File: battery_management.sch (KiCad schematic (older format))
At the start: 8 parts

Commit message: Finally finished final draft
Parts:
- gave numbers to parts that had none: 8
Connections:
- net charging/VCC_IN_USB renamed charging_ic/VCC_IN_USB
- net fuel_gage/VCC_BAT renamed fuel_gage_ic/VCC_BAT
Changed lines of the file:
@@
 P 7100 2900
 AR Path="/60C0E79E" Ref="C?"  Part="1"
-AR Path="/60BA4931/60C0E79E" Ref="C?"  Part="1"
-F 0 "C?" H 7215 2946 50  0000 L CNN
+AR Path="/60BA4931/60C0E79E" Ref="C7"  Part="1"
+F 0 "C7" H 7215 2946 50  0000 L CNN
 F 1 "0.1uF" H 7215 2855 50  0000 L CNN
 F 2 "" H 7138 2750 50  0001 C CNN
@@
 P 7650 2900
 AR Path="/60C0E7AB" Ref="C?"  Part="1"
-AR Path="/60BA4931/60C0E7AB" Ref="C?"  Part="1"
-F 0 "C?" H 7765 2946 50  0000 L CNN
+AR Path="/60BA4931/60C0E7AB" Ref="C6"  Part="1"
+F 0 "C6" H 7765 2946 50  0000 L CNN
 F 1 "10uF" H 7765 2855 50  0000 L CNN
 F 2 "" H 7688 2750 50  0001 C CNN
@@
 P 8150 2900
 AR Path="/60C0E7BA" Ref="C?"  Part="1"
-AR Path="/60BA4931/60C0E7BA" Ref="C?"  Part="1"
-F 0 "C?" H 8265 2946 50  0000 L CNN
+AR Path="/60BA4931/60C0E7BA" Ref="C5"  Part="1"
+F 0 "C5" H 8265 2946 50  0000 L CNN
 F 1 "10uF" H 8265 2855 50  0000 L CNN
 F 2 "" H 8188 2750 50  0001 C CNN
@@
 P 8700 2900
 AR Path="/60C0E7C0" Ref="C?"  Part="1"
-AR Path="/60BA4931/60C0E7C0" Ref="C?"  Part="1"
-F 0 "C?" H 8815 2946 50  0000 L CNN
+AR Path="/60BA4931/60C0E7C0" Ref="C4"  Part="1"
+F 0 "C4" H 8815 2946 50  0000 L CNN
 F 1 "0.1uF" H 8815 2855 50  0000 L CNN
 F 2 "" H 8738 2750 50  0001 C CNN
@@
 P 7900 2600
 AR Path="/60C0E7D7" Ref="FB?"  Part="1"
-AR Path="/60BA4931/60C0E7D7" Ref="FB?"  Part="1"
-F 0 "FB?" V 7626 2600 50  0000 C CNN
+AR Path="/60BA4931/60C0E7D7" Ref="FB1"  Part="1"
+F 0 "FB1" V 7626 2600 50  0000 C CNN
 F 1 "FerriteBead" V 7717 2600 50  0000 C CNN
 F 2 "" V 7830 2600 50  0001 C CNN
@@
 F3 "VCC_IN" I L 5700 3400 50
 $EndSheet
-$Sheet
-S 2400 3100 1150 1350
-U 60C6FA96
-F0 "fuel_gage" 50
-F1 "fuel_gage.sch" 50
-F2 "VCC_3V3" I R 3550 3850 50
-F3 "GPOUT" O R 3550 4050 50
-F4 "SCL" I R 3550 4250 50
-F5 "SDA" B R 3550 4150 50
-F6 "VCC_BAT" B L 2400 3750 50
-F7 "VCC_LOAD_OR_CHARGE" B R 3550 3300 50
-$EndSheet
-$Sheet
-S 4050 2450 1100 550
-U 60C34886
-F0 "charging" 50
-F1 "charging.sch" 50
-F2 "VCC_LOAD" O R 5150 2600 50
-F3 "VCC_IN_USB" I L 4050 2600 50
-F4 "VCC_BAT_OR_CHARGE" B L 4050 2850 50
-$EndSheet
 Wire Wire Line
 	5150 2600 5400 2600
@@
 P 1750 3850
 AR Path="/60C8C86F" Ref="J?"  Part="1"
-AR Path="/60BA4931/60C8C86F" Ref="J?"  Part="1"
+AR Path="/60BA4931/60C8C86F" Ref="J7"  Part="1"
 AR Path="/60BA4931/60C6FA96/60C8C86F" Ref="J?"  Part="1"
-F 0 "J?" H 1668 3525 50  0000 C CNN
+F 0 "J7" H 1668 3525 50  0000 C CNN
 F 1 "Battery_175mAh" H 1668 3616 50  0000 C CNN
 F 2 "" H 1750 3850 50  0001 C CNN
@@
 P 1800 1650
 AR Path="/60C9133A" Ref="J?"  Part="1"
-AR Path="/60BA4931/60C9133A" Ref="J?"  Part="1"
+AR Path="/60BA4931/60C9133A" Ref="J6"  Part="1"
 AR Path="/60BA4931/60C34886/60C9133A" Ref="J?"  Part="1"
-F 0 "J?" H 1857 2117 50  0000 C CNN
+F 0 "J6" H 1857 2117 50  0000 C CNN
 F 1 "USB_B_Micro" H 1857 2026 50  0000 C CNN
 F 2 "" H 1950 1600 50  0001 C CNN
@@
 P 2450 1750
 AR Path="/60C91355" Ref="D?"  Part="1"
-AR Path="/60BA4931/60C91355" Ref="D?"  Part="1"
+AR Path="/60BA4931/60C91355" Ref="D1"  Part="1"
 AR Path="/60BA4931/60C34886/60C91355" Ref="D?"  Part="1"
-F 0 "D?" V 2404 1880 50  0000 L CNN
+F 0 "D1" V 2404 1880 50  0000 L CNN
 F 1 "SMAJ5.0A" V 2495 1880 50  0000 L CNN
 F 2 "DIOM5026X229N" H 2200 1500 50  0001 L CNN
@@
 Text HLabel 9000 2600 2    50   Output ~ 0
 VCC_POWER
+Wire Wire Line
+	3550 4050 3950 4050
+Wire Wire Line
+	3550 4150 3950 4150
+Wire Wire Line
+	3550 4250 3950 4250
+Text HLabel 3950 4050 2    50   Output ~ 0
+GPOUT
+Text HLabel 3950 4150 2    50   BiDi ~ 0
+SDA
+Text HLabel 3950 4250 2    50   Input ~ 0
+SCL
+$Sheet
+S 4050 2450 1100 550
+U 60C34886
+F0 "charging_ic" 50
+F1 "charging_ic.sch" 50
+F2 "VCC_LOAD" O R 5150 2600 50
+F3 "VCC_IN_USB" I L 4050 2600 50
+F4 "VCC_BAT_OR_CHARGE" B L 4050 2850 50
+$EndSheet
+$Sheet
+S 2400 3100 1150 1350
+U 60C6FA96
+F0 "fuel_gage_ic" 50
+F1 "fuel_gage_ic.sch" 50
+F2 "VCC_3V3" I R 3550 3850 50
+F3 "GPOUT" O R 3550 4050 50
+F4 "SCL" I R 3550 4250 50
+F5 "SDA" B R 3550 4150 50
+F6 "VCC_BAT" B L 2400 3750 50
+F7 "VCC_LOAD_OR_CHARGE" B R 3550 3300 50
+$EndSheet
 $EndSCHEMATC

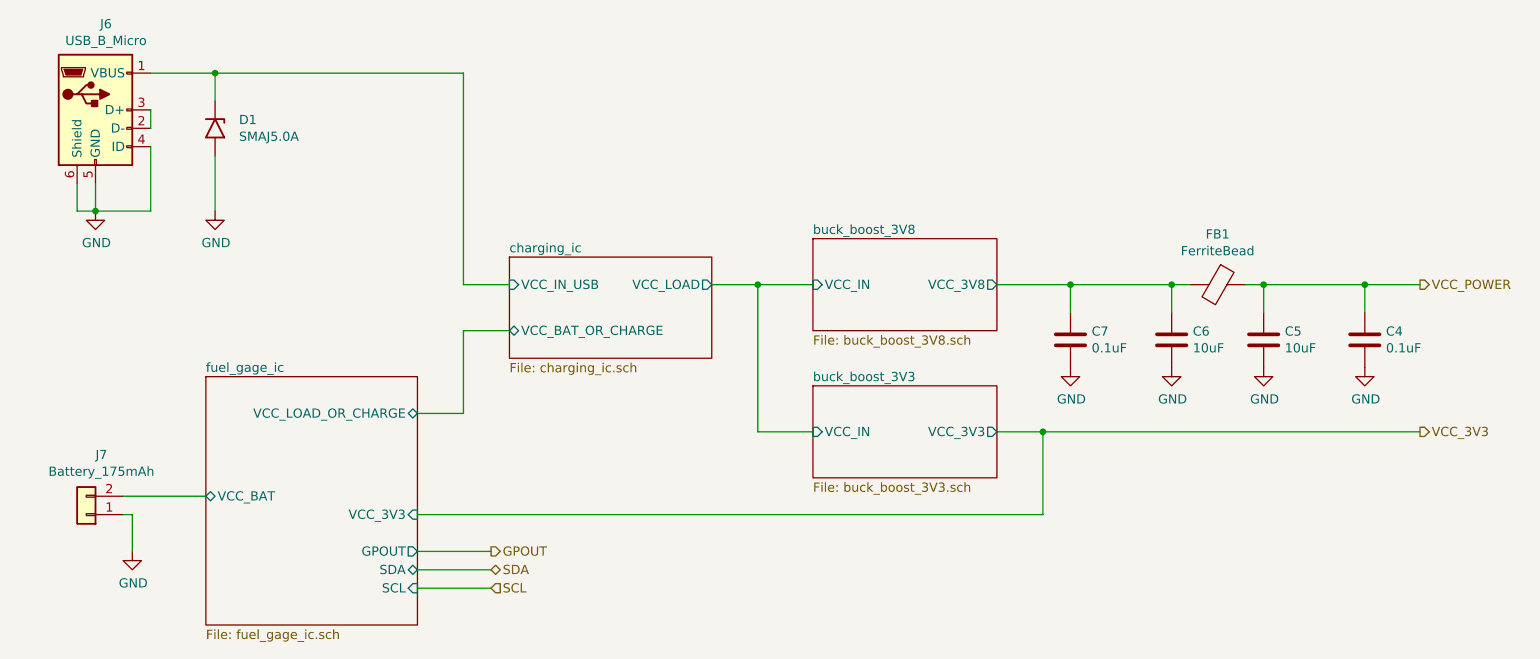
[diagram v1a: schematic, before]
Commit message: Fixed some symbols, assigned some footprints, and made wire labels
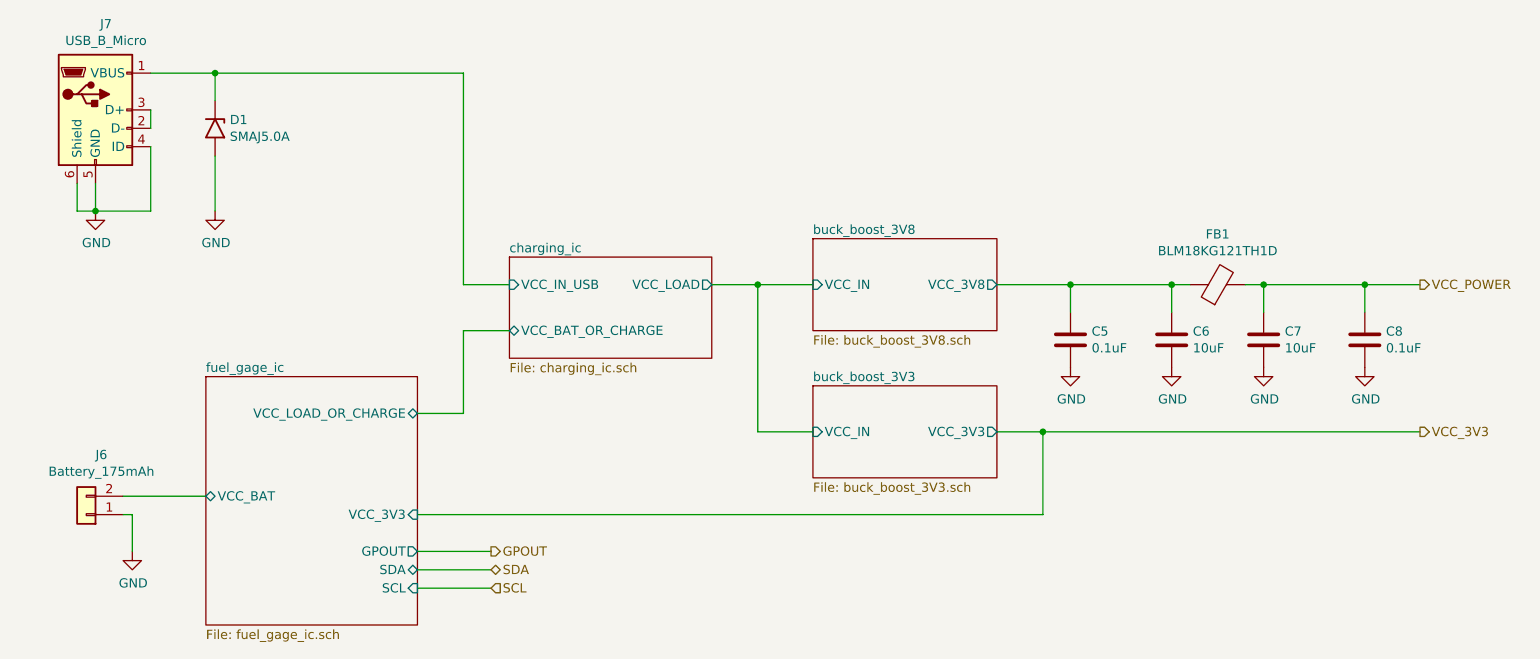
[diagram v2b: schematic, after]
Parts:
- removed FB1: FerriteBead, symbol Device:FerriteBead
- added FB1: BLM18KG121TH1D, Ferrite_Skywire:BLM18KG101TH1D, symbol Ferrite_Bead:BLM18KG121TH1D
- D1: footprint DIOM5026X229N -> Diode_Skywire:DIOM5026X229N
- renumbered C7 to C5, C5 to C7, C4 to C8, J7 to J6, J6 to J7
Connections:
- net VCC_POWER: now also FB1.2
- net buck_boost_3V8/VCC_3V8: now also FB1.1
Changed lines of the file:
@@
 P 7100 2900
 AR Path="/60C0E79E" Ref="C?"  Part="1"
-AR Path="/60BA4931/60C0E79E" Ref="C7"  Part="1"
-F 0 "C7" H 7215 2946 50  0000 L CNN
+AR Path="/60BA4931/60C0E79E" Ref="C5"  Part="1"
+F 0 "C5" H 7215 2946 50  0000 L CNN
 F 1 "0.1uF" H 7215 2855 50  0000 L CNN
 F 2 "" H 7138 2750 50  0001 C CNN
@@
 P 7100 3050
 AR Path="/60C0E7A4" Ref="#PWR?"  Part="1"
-AR Path="/60BA4931/60C0E7A4" Ref="#PWR?"  Part="1"
-F 0 "#PWR?" H 7100 2800 50  0001 C CNN
+AR Path="/60BA4931/60C0E7A4" Ref="#PWR012"  Part="1"
+F 0 "#PWR012" H 7100 2800 50  0001 C CNN
 F 1 "GND" H 7105 2877 50  0000 C CNN
 F 2 "" H 7100 3050 50  0001 C CNN
@@
 P 7650 3050
 AR Path="/60C0E7B1" Ref="#PWR?"  Part="1"
-AR Path="/60BA4931/60C0E7B1" Ref="#PWR?"  Part="1"
-F 0 "#PWR?" H 7650 2800 50  0001 C CNN
+AR Path="/60BA4931/60C0E7B1" Ref="#PWR013"  Part="1"
+F 0 "#PWR013" H 7650 2800 50  0001 C CNN
 F 1 "GND" H 7655 2877 50  0000 C CNN
 F 2 "" H 7650 3050 50  0001 C CNN
@@
 P 8150 2900
 AR Path="/60C0E7BA" Ref="C?"  Part="1"
-AR Path="/60BA4931/60C0E7BA" Ref="C5"  Part="1"
-F 0 "C5" H 8265 2946 50  0000 L CNN
+AR Path="/60BA4931/60C0E7BA" Ref="C7"  Part="1"
+F 0 "C7" H 8265 2946 50  0000 L CNN
 F 1 "10uF" H 8265 2855 50  0000 L CNN
 F 2 "" H 8188 2750 50  0001 C CNN
@@
 P 8700 2900
 AR Path="/60C0E7C0" Ref="C?"  Part="1"
-AR Path="/60BA4931/60C0E7C0" Ref="C4"  Part="1"
-F 0 "C4" H 8815 2946 50  0000 L CNN
+AR Path="/60BA4931/60C0E7C0" Ref="C8"  Part="1"
+F 0 "C8" H 8815 2946 50  0000 L CNN
 F 1 "0.1uF" H 8815 2855 50  0000 L CNN
 F 2 "" H 8738 2750 50  0001 C CNN
@@
 P 8150 3050
 AR Path="/60C0E7C6" Ref="#PWR?"  Part="1"
-AR Path="/60BA4931/60C0E7C6" Ref="#PWR?"  Part="1"
-F 0 "#PWR?" H 8150 2800 50  0001 C CNN
+AR Path="/60BA4931/60C0E7C6" Ref="#PWR014"  Part="1"
+F 0 "#PWR014" H 8150 2800 50  0001 C CNN
 F 1 "GND" H 8155 2877 50  0000 C CNN
 F 2 "" H 8150 3050 50  0001 C CNN
@@
 P 8700 3050
 AR Path="/60C0E7CC" Ref="#PWR?"  Part="1"
-AR Path="/60BA4931/60C0E7CC" Ref="#PWR?"  Part="1"
-F 0 "#PWR?" H 8700 2800 50  0001 C CNN
+AR Path="/60BA4931/60C0E7CC" Ref="#PWR015"  Part="1"
+F 0 "#PWR015" H 8700 2800 50  0001 C CNN
 F 1 "GND" H 8705 2877 50  0000 C CNN
 F 2 "" H 8700 3050 50  0001 C CNN
@@
 Wire Wire Line
 	8700 2600 9000 2600
-$Comp
-L Device:FerriteBead FB?
-U 1 1 60C0E7D7
-P 7900 2600
-AR Path="/60C0E7D7" Ref="FB?"  Part="1"
-AR Path="/60BA4931/60C0E7D7" Ref="FB1"  Part="1"
-F 0 "FB1" V 7626 2600 50  0000 C CNN
-F 1 "FerriteBead" V 7717 2600 50  0000 C CNN
-F 2 "" V 7830 2600 50  0001 C CNN
-F 3 "~" H 7900 2600 50  0001 C CNN
-	1    7900 2600
-	0    1    1    0
-$EndComp
 Wire Wire Line
 	8050 2600 8150 2600
@@
 P 1750 3850
 AR Path="/60C8C86F" Ref="J?"  Part="1"
-AR Path="/60BA4931/60C8C86F" Ref="J7"  Part="1"
+AR Path="/60BA4931/60C8C86F" Ref="J6"  Part="1"
 AR Path="/60BA4931/60C6FA96/60C8C86F" Ref="J?"  Part="1"
-F 0 "J7" H 1668 3525 50  0000 C CNN
+F 0 "J6" H 1668 3525 50  0000 C CNN
 F 1 "Battery_175mAh" H 1668 3616 50  0000 C CNN
 F 2 "" H 1750 3850 50  0001 C CNN
@@
 	2000 3850 2000 4050
 $Comp
-L power:GND #PWR?
+L power:GND #PWR010
 U 1 1 60C8D052
 P 2000 4050
-F 0 "#PWR?" H 2000 3800 50  0001 C CNN
+F 0 "#PWR010" H 2000 3800 50  0001 C CNN
 F 1 "GND" H 2005 3877 50  0000 C CNN
 F 2 "" H 2000 4050 50  0001 C CNN
@@
 P 1800 1650
 AR Path="/60C9133A" Ref="J?"  Part="1"
-AR Path="/60BA4931/60C9133A" Ref="J6"  Part="1"
+AR Path="/60BA4931/60C9133A" Ref="J7"  Part="1"
 AR Path="/60BA4931/60C34886/60C9133A" Ref="J?"  Part="1"
-F 0 "J6" H 1857 2117 50  0000 C CNN
+F 0 "J7" H 1857 2117 50  0000 C CNN
 F 1 "USB_B_Micro" H 1857 2026 50  0000 C CNN
 F 2 "" H 1950 1600 50  0001 C CNN
@@
 P 1800 2200
 AR Path="/60C91347" Ref="#PWR?"  Part="1"
-AR Path="/60BA4931/60C91347" Ref="#PWR?"  Part="1"
+AR Path="/60BA4931/60C91347" Ref="#PWR09"  Part="1"
 AR Path="/60BA4931/60C34886/60C91347" Ref="#PWR?"  Part="1"
-F 0 "#PWR?" H 1800 1950 50  0001 C CNN
+F 0 "#PWR09" H 1800 1950 50  0001 C CNN
 F 1 "GND" H 1805 2027 50  0000 C CNN
 F 2 "" H 1800 2200 50  0001 C CNN
@@
 	1    0    0    -1
 $EndComp
-$Comp
-L Diode_TVS:SMAJ5.0A D?
-U 1 1 60C91355
-P 2450 1750
-AR Path="/60C91355" Ref="D?"  Part="1"
-AR Path="/60BA4931/60C91355" Ref="D1"  Part="1"
-AR Path="/60BA4931/60C34886/60C91355" Ref="D?"  Part="1"
-F 0 "D1" V 2404 1880 50  0000 L CNN
-F 1 "SMAJ5.0A" V 2495 1880 50  0000 L CNN
-F 2 "DIOM5026X229N" H 2200 1500 50  0001 L CNN
-F 3 "https://detail.tmall.com/item.htm?id=548354020241&ali_refid=a3_430583_1006:1109983619:N:3Uw9kZ3UMDT/QL57nh1fXA==:ab063b49c94624768a940a913313feb0&ali_trackid=1_ab063b49c94624768a940a913313feb0&spm=a230r.1.14.1" H 2200 1400 50  0001 L CNN
-F 4 "BOURNS - SMAJ5.0A - TVS Diode, TRANSZORB SMAJ Series, Unidirectional, 5 V, 9.2 V, DO-214AC (SMA), 2 Pins" H 2200 1300 50  0001 L CNN "Description"
-F 5 "2.29" H 2200 1200 50  0001 L CNN "Height"
-F 6 "Bourns" H 2200 1100 50  0001 L CNN "Manufacturer_Name"
-F 7 "SMAJ5.0A" H 2200 1000 50  0001 L CNN "Manufacturer_Part_Number"
-F 8 "652-SMAJ5.0A" H 2200 900 50  0001 L CNN "Mouser Part Number"
-F 9 "https://www.mouser.co.uk/ProductDetail/Bourns/SMAJ50A?qs=A3H9pljuJ8RbLIvzFxDfUA%3D%3D" H 2200 800 50  0001 L CNN "Mouser Price/Stock"
-F 10 "SMAJ5.0A" H 2200 700 50  0001 L CNN "Arrow Part Number"
-F 11 "https://www.arrow.com/en/products/smaj5.0a/bourns" H 2200 600 50  0001 L CNN "Arrow Price/Stock"
-	1    2450 1750
-	0    1    1    0
-$EndComp
 Wire Wire Line
 	2450 1450 2450 1600
@@
 P 2450 2200
 AR Path="/60C9135D" Ref="#PWR?"  Part="1"
-AR Path="/60BA4931/60C9135D" Ref="#PWR?"  Part="1"
+AR Path="/60BA4931/60C9135D" Ref="#PWR011"  Part="1"
 AR Path="/60BA4931/60C34886/60C9135D" Ref="#PWR?"  Part="1"
-F 0 "#PWR?" H 2450 1950 50  0001 C CNN
+F 0 "#PWR011" H 2450 1950 50  0001 C CNN
 F 1 "GND" H 2455 2027 50  0000 C CNN
 F 2 "" H 2450 2200 50  0001 C CNN
@@
 F7 "VCC_LOAD_OR_CHARGE" B R 3550 3300 50
 $EndSheet
+$Comp
+L Diode_TVS:SMAJ5.0A D1
+U 1 1 60784817
+P 2450 1750
+F 0 "D1" V 2404 1830 50  0000 L CNN
+F 1 "SMAJ5.0A" V 2495 1830 50  0000 L CNN
+F 2 "Diode_Skywire:DIOM5026X229N" H 2100 1600 50  0001 L CNN
+F 3 "https://detail.tmall.com/item.htm?id=548354020241&ali_refid=a3_430583_1006:1109983619:N:3Uw9kZ3UMDT/QL57nh1fXA==:ab063b49c94624768a940a913313feb0&ali_trackid=1_ab063b49c94624768a940a913313feb0&spm=a230r.1.14.1" H 2100 1500 50  0001 L CNN
+F 4 "BOURNS - SMAJ5.0A - TVS Diode, TRANSZORB SMAJ Series, Unidirectional, 5 V, 9.2 V, DO-214AC (SMA), 2 Pins" H 2100 1400 50  0001 L CNN "Description"
+F 5 "2.29" H 2100 1300 50  0001 L CNN "Height"
+F 6 "Bourns" H 2100 1200 50  0001 L CNN "Manufacturer_Name"
+F 7 "SMAJ5.0A" H 2100 1100 50  0001 L CNN "Manufacturer_Part_Number"
+F 8 "652-SMAJ5.0A" H 2100 1000 50  0001 L CNN "Mouser Part Number"
+F 9 "https://www.mouser.co.uk/ProductDetail/Bourns/SMAJ50A?qs=A3H9pljuJ8RbLIvzFxDfUA%3D%3D" H 2100 900 50  0001 L CNN "Mouser Price/Stock"
+F 10 "SMAJ5.0A" H 2100 800 50  0001 L CNN "Arrow Part Number"
+F 11 "https://www.arrow.com/en/products/smaj5.0a/bourns" H 2100 700 50  0001 L CNN "Arrow Price/Stock"
+	1    2450 1750
+	0    1    1    0
+$EndComp
+$Comp
+L Ferrite_Bead:BLM18KG121TH1D FB1
+U 1 1 6066ADBC
+P 7900 2600
+F 0 "FB1" H 7900 2874 50  0000 C CNN
+F 1 "BLM18KG121TH1D" H 7900 2783 50  0000 C CNN
+F 2 "Ferrite_Skywire:BLM18KG101TH1D" H 7550 2350 50  0001 L CNN
+F 3 "https://www.murata.com/en-us/products/productdetail?partno=BLM18KG121TH1%23" H 7550 2250 50  0001 L CNN
+F 4 "BLM18_H1D Series EMI Suppression Filter 120+/-25% at 100MHz 3A @85" H 7550 2150 50  0001 L CNN "Description"
+F 5 "0.75" H 7550 2050 50  0001 L CNN "Height"
+F 6 "Murata Electronics" H 7550 1950 50  0001 L CNN "Manufacturer_Name"
+F 7 "BLM18KG121TH1D" H 7550 1850 50  0001 L CNN "Manufacturer_Part_Number"
+F 8 "81-BLM18KG121TH1D" H 7550 1750 50  0001 L CNN "Mouser Part Number"
+F 9 "https://www.mouser.co.uk/ProductDetail/Murata-Electronics/BLM18KG121TH1D/?qs=DXqDLUyyb5VDoB6j6ePjSQ%3D%3D" H 7550 1650 50  0001 L CNN "Mouser Price/Stock"
+F 10 "BLM18KG121TH1D" H 7550 1550 50  0001 L CNN "Arrow Part Number"
+F 11 "https://www.arrow.com/en/products/blm18kg121th1d/murata-manufacturing" H 7550 1450 50  0001 L CNN "Arrow Price/Stock"
+	1    7900 2600
+	1    0    0    -1
+$EndComp
 $EndSCHEMATC

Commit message: Finished annotations and assigned more footprints, electrical rules check is marked good
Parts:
- removed J6: Battery_175mAh, symbol Connector_Generic:Conn_01x02
- added J6: S2B-PH-K-S_LF__SN_, Connector_Skywire:SHDRRA2W50P0X200_1X2_590X760X480P, symbol Connector_JST_2PIN:S2B-PH-K-S_LF__SN_
- J7: footprint (none) -> Connector_USB:USB_Micro-B_Amphenol_10103594-0001LF_Horizontal
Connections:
- net GND: now also J6.1 (Pin_1)
- net fuel_gage_ic/VCC_BAT: now also J6.2 (Pin_2)
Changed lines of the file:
@@
 Wire Wire Line
 	6950 3400 6950 3850
-$Comp
-L Connector_Generic:Conn_01x02 J?
-U 1 1 60C8C86F
-P 1750 3850
-AR Path="/60C8C86F" Ref="J?"  Part="1"
-AR Path="/60BA4931/60C8C86F" Ref="J6"  Part="1"
-AR Path="/60BA4931/60C6FA96/60C8C86F" Ref="J?"  Part="1"
-F 0 "J6" H 1668 3525 50  0000 C CNN
-F 1 "Battery_175mAh" H 1668 3616 50  0000 C CNN
-F 2 "" H 1750 3850 50  0001 C CNN
-F 3 "~" H 1750 3850 50  0001 C CNN
-	1    1750 3850
-	-1   0    0    1
-$EndComp
 Wire Wire Line
 	1950 3850 2000 3850
@@
 F 0 "J7" H 1857 2117 50  0000 C CNN
 F 1 "USB_B_Micro" H 1857 2026 50  0000 C CNN
-F 2 "" H 1950 1600 50  0001 C CNN
+F 2 "Connector_USB:USB_Micro-B_Amphenol_10103594-0001LF_Horizontal" H 1950 1600 50  0001 C CNN
 F 3 "~" H 1950 1600 50  0001 C CNN
 	1    1800 1650
@@
 	1    0    0    -1
 $EndComp
+$Comp
+L Connector_JST_2PIN:S2B-PH-K-S_LF__SN_ J6
+U 1 1 60683BAA
+P 1750 3800
+F 0 "J6" H 1668 3525 50  0000 C CNN
+F 1 "S2B-PH-K-S_LF__SN_" H 1668 3616 50  0000 C CNN
+F 2 "Connector_Skywire:SHDRRA2W50P0X200_1X2_590X760X480P" H 1350 3600 50  0001 L CNN
+F 3 "http://uk.rs-online.com/web/p/products/8201494" H 1350 3500 50  0001 L CNN
+F 4 "PH-2.0mm Header side entry 2 way JST PH Series, Series Number S2B, 2mm Pitch 2 Way 1 Row Right Angle PCB Header, Through Hole Termination, 2A" H 1350 3400 50  0001 L CNN "Description"
+F 5 "4.8" H 1350 3300 50  0001 L CNN "Height"
+F 6 "JST (JAPAN SOLDERLESS TERMINALS)" H 1350 3200 50  0001 L CNN "Manufacturer_Name"
+F 7 "S2B-PH-K-S(LF)(SN)" H 1350 3100 50  0001 L CNN "Manufacturer_Part_Number"
+F 8 "S2B-PH-K-S(LF)(SN)" H 1350 2800 50  0001 L CNN "Arrow Part Number"
+F 9 "https://www.arrow.com/en/products/s2b-ph-k-s-lf-sn/jst-manufacturing" H 1350 2700 50  0001 L CNN "Arrow Price/Stock"
+	1    1750 3800
+	-1   0    0    1
+$EndComp
 $EndSCHEMATC

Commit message: Finished assigning footprints, and generated netlist
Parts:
- C5, C8: footprint (none) -> Capacitor_SMD:C_0603_1608Metric
- C6, C7: footprint (none) -> Capacitor_SMD:C_0805_2012Metric
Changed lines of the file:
@@
 F 0 "C5" H 7215 2946 50  0000 L CNN
 F 1 "0.1uF" H 7215 2855 50  0000 L CNN
-F 2 "" H 7138 2750 50  0001 C CNN
+F 2 "Capacitor_SMD:C_0603_1608Metric" H 7138 2750 50  0001 C CNN
 F 3 "~" H 7100 2900 50  0001 C CNN
 	1    7100 2900
@@
 F 0 "C6" H 7765 2946 50  0000 L CNN
 F 1 "10uF" H 7765 2855 50  0000 L CNN
-F 2 "" H 7688 2750 50  0001 C CNN
+F 2 "Capacitor_SMD:C_0805_2012Metric" H 7688 2750 50  0001 C CNN
 F 3 "~" H 7650 2900 50  0001 C CNN
 	1    7650 2900
@@
 F 0 "C7" H 8265 2946 50  0000 L CNN
 F 1 "10uF" H 8265 2855 50  0000 L CNN
-F 2 "" H 8188 2750 50  0001 C CNN
+F 2 "Capacitor_SMD:C_0805_2012Metric" H 8188 2750 50  0001 C CNN
 F 3 "~" H 8150 2900 50  0001 C CNN
 	1    8150 2900
@@
 F 0 "C8" H 8815 2946 50  0000 L CNN
 F 1 "0.1uF" H 8815 2855 50  0000 L CNN
-F 2 "" H 8738 2750 50  0001 C CNN
+F 2 "Capacitor_SMD:C_0603_1608Metric" H 8738 2750 50  0001 C CNN
 F 3 "~" H 8700 2900 50  0001 C CNN
 	1    8700 2900
